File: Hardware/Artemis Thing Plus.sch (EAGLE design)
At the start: 65 parts, among them J2 CORTEX_DEBUG, J5 USB-C, U1 MCP73831, U2 3.3V, U3 ARTEMIS_MODULESMD, U4 CH340E_MSOP10, Y1 32.768kHz

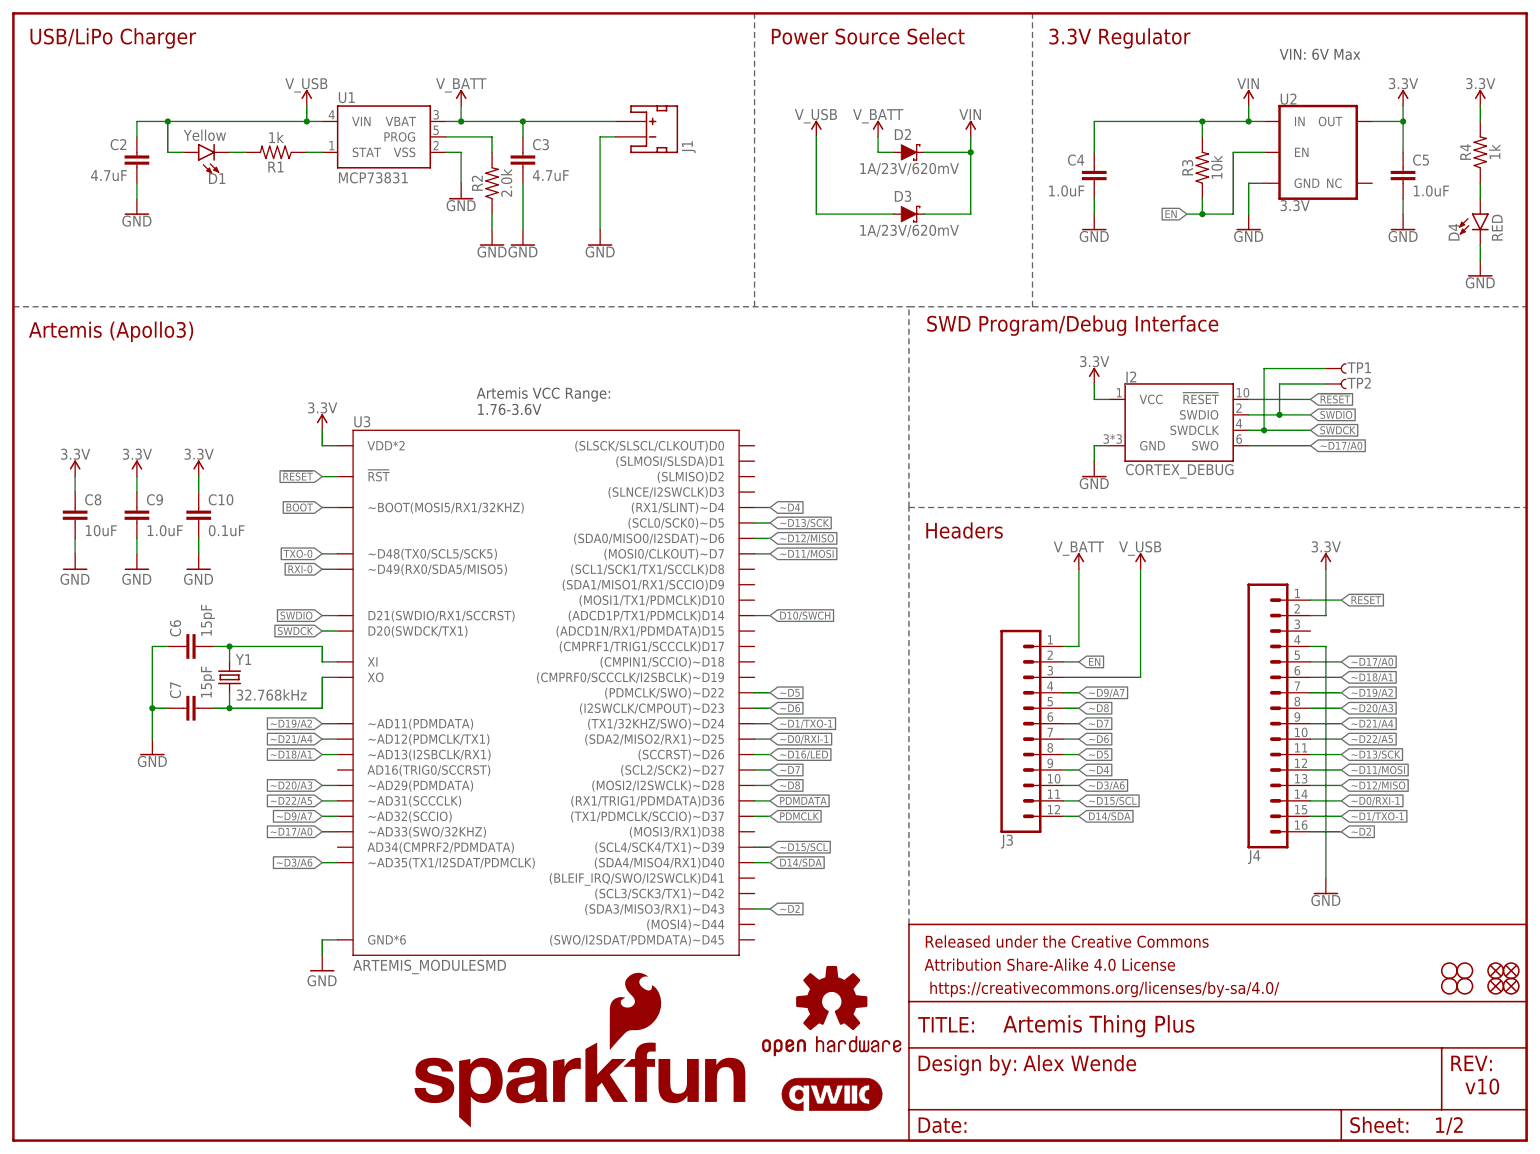
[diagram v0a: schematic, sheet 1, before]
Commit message: v10 Update
Schematic:
- Change 100k pull-down resistor in bootloader circuit to DNP
- Replaced diodes with lower forward voltage drop
- Added second I2C Bus to breakout pins. All broken out pins are now PWM capable
- Replaced 4.7k LEDs resistors to 1k for all LEDs
- Added testpoints for Qwiic data lines

Layout:
- Removed "~" for PWM pins as all pins now support PWM
- Increased flame logo
- Fixed USB traces
- Labeled microphone
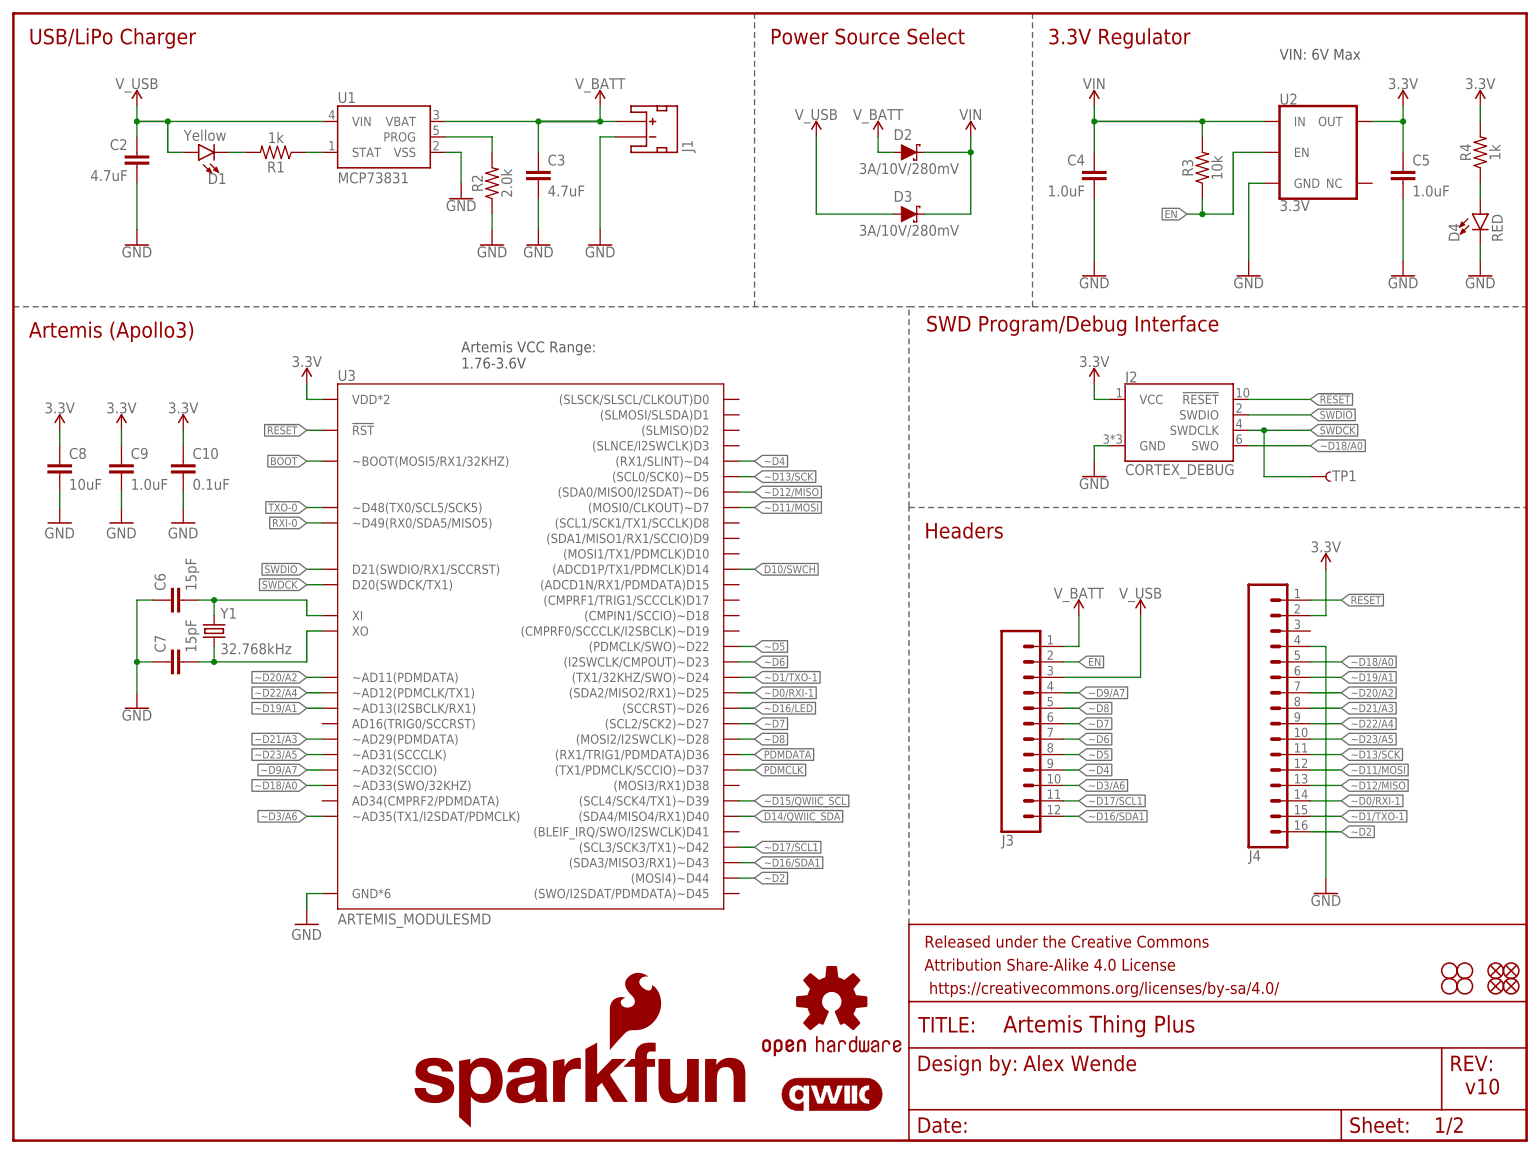
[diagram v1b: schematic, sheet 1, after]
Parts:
- added TP5: TEST-POINTTP_15TH_THRU, SparkFun-Connectors:TEST-POINTTP_15TH_THRU
- D2, D3: value 1A/23V/620mV -> 3A/10V/280mV; device SparkFun-DiscreteSemi:DIODE-SCHOTTKY-BAT20J -> SparkFun-DiscreteSemi:DIODE-SCHOTTKY-BAT60A
- R7, R8: value 4.7k -> 1k; device SparkFun-Resistors:4.7KOHM-0603-1/10W-1% -> SparkFun-Resistors:1KOHM-0603-1/10W-1%
- R9: value 100k -> DNP
- TP1, TP2, TP3, TP4: value TEST-POINT3 -> TEST-POINTTP_15TH_THRU; device SparkFun-Connectors:TEST-POINT3 -> SparkFun-Connectors:TEST-POINTTP_15TH_THRU
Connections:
- net ~D17/A0 renamed ~D18/A0
- net ~D18/A1 renamed ~D19/A1
- net ~D19/A2 renamed ~D20/A2
- net ~D20/A3 renamed ~D21/A3
- net ~D21/A4 renamed ~D22/A4
- net ~D22/A5 renamed ~D23/A5
- removed net D14/SDA: J3.12, J6.3, U3.(SDA4/MISO4/RX1)D40
- removed net ~D15/SCL: J3.11, J6.4, U3.(SCL4/SCK4/TX1)~D39
- new net D14/QWIIC_SDA: J6.3, TP5.1, U3.(SDA4/MISO4/RX1)D40
- new net ~D15/QWIIC_SCL: J6.4, TP4.1, U3.(SCL4/SCK4/TX1)~D39
- new net ~D16/SDA1: J3.12, U3.(SDA3/MISO3/RX1)~D43
- new net ~D17/SCL1: J3.11, U3.(SCL3/SCK3/TX1)~D42
- net RXI-0: now also TP2.1; no longer TP3.1
- net SWDIO: no longer TP2.1
- net TXO-0: now also TP3.1; no longer TP4.1
- net ~D2: now also U3.(MOSI4)~D44; no longer U3.(SDA3/MISO3/RX1)~D43
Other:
- moved on the sheet: C1, C10, C3, C6, C7, C8, C9, TP1, TP3, TP4, U3, Y1

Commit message: v10 design review changes
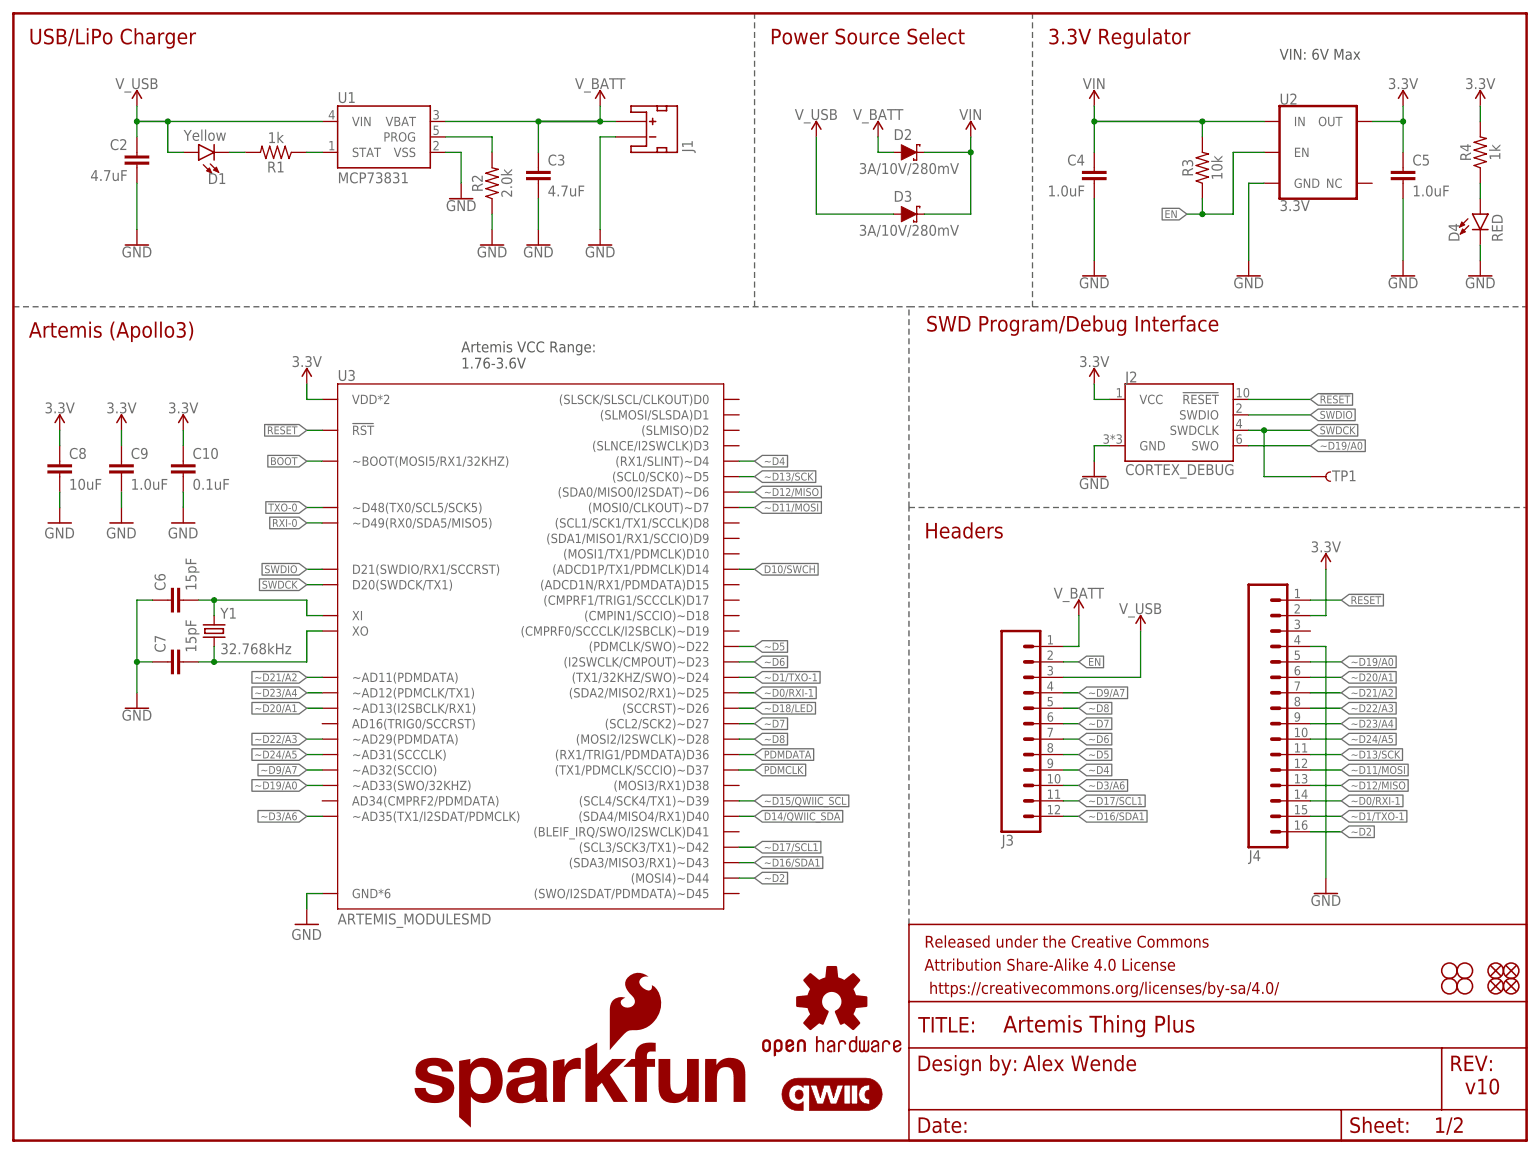
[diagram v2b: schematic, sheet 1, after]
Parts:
- removed R9: DNP, SparkFun-Resistors:100KOHM-0603-1/10W-1%
- C13: value 2.2uF -> 0.1uF; device SparkFun-Capacitors:2.2UF-0603-10V-20% -> SparkFun-Capacitors:0.1UF-0603-25V-5%
- R10: value 10k -> 220k; device SparkFun-Resistors:10KOHM-0603-1/10W-1% -> SparkFun-Resistors:220KOHM-0603-1/10W-1%
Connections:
- net ~D16/LED renamed ~D18/LED
- net ~D18/A0 renamed ~D19/A0
- net ~D19/A1 renamed ~D20/A1
- net ~D20/A2 renamed ~D21/A2
- net ~D21/A3 renamed ~D22/A3
- net ~D22/A4 renamed ~D23/A4
- net ~D23/A5 renamed ~D24/A5
- net !RTS: no longer R9.2
- net GND: no longer R9.1
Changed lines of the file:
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@@
 <part name="C14" library="SparkFun-Capacitors" deviceset="0.1UF" device="-0603-25V-5%" value="0.1uF"/>
 <part name="GND41" library="SparkFun-PowerSymbols" deviceset="GND" device=""/>
-<part name="R10" library="SparkFun-Resistors" deviceset="10KOHM" device="-0603-1/10W-1%" value="10k"/>
-<part name="C13" library="SparkFun-Capacitors" deviceset="2.2UF" device="-0603-10V-20%" value="2.2uF"/>
-<part name="R9" library="SparkFun-Resistors" deviceset="100KOHM" device="-0603-1/10W-1%" value="DNP"/>
-<part name="GND44" library="SparkFun-PowerSymbols" deviceset="GND" device=""/>
+<part name="R10" library="SparkFun-Resistors" deviceset="220KOHM" device="-0603-1/10W-1%" value="220k"/>
+<part name="C13" library="SparkFun-Capacitors" deviceset="0.1UF" device="-0603-25V-5%" value="0.1uF"/>
 <part name="C15" library="SparkFun-Capacitors" deviceset="1.0NF/1000PF" device="-0603-50V-10%" value="1nF"/>
 <part name="GND45" library="SparkFun-PowerSymbols" deviceset="GND" device=""/>
@@
 <attribute name="VALUE" x="175.26" y="89.154" size="1.778" layer="96" font="vector" align="bottom-center"/>
 </instance>
-<instance part="SUPPLY17" gate="G$1" x="185.42" y="86.36" smashed="yes">
-<attribute name="VALUE" x="185.42" y="89.154" size="1.778" layer="96" font="vector" align="bottom-center"/>
+<instance part="SUPPLY17" gate="G$1" x="185.42" y="83.82" smashed="yes">
+<attribute name="VALUE" x="185.42" y="86.614" size="1.778" layer="96" font="vector" align="bottom-center"/>
 </instance>
 </instances>
@@
 <pinref part="J3" gate="G$1" pin="3"/>
 <pinref part="SUPPLY17" gate="G$1" pin="V_USB"/>
-<wire x1="185.42" y1="86.36" x2="185.42" y2="76.2" width="0.1524" layer="91"/>
+<wire x1="185.42" y1="83.82" x2="185.42" y2="76.2" width="0.1524" layer="91"/>
 <wire x1="185.42" y1="76.2" x2="172.72" y2="76.2" width="0.1524" layer="91"/>
 </segment>
@@
 </segment>
 </net>
-<net name="~D22/A4" class="0">
+<net name="~D23/A4" class="0">
 <segment>
 <wire x1="50.8" y1="73.66" x2="48.26" y2="73.66" width="0.1524" layer="91"/>
@@
 </segment>
 </net>
-<net name="~D23/A5" class="0">
+<net name="~D24/A5" class="0">
 <segment>
 <wire x1="50.8" y1="63.5" x2="48.26" y2="63.5" width="0.1524" layer="91"/>
@@
 </segment>
 </net>
-<net name="~D21/A3" class="0">
+<net name="~D22/A3" class="0">
 <segment>
 <wire x1="50.8" y1="66.04" x2="48.26" y2="66.04" width="0.1524" layer="91"/>
@@
 </segment>
 </net>
-<net name="~D20/A2" class="0">
+<net name="~D21/A2" class="0">
 <segment>
 <wire x1="50.8" y1="76.2" x2="48.26" y2="76.2" width="0.1524" layer="91"/>
@@
 </segment>
 </net>
-<net name="~D18/A0" class="0">
+<net name="~D19/A0" class="0">
 <segment>
 <wire x1="50.8" y1="58.42" x2="48.26" y2="58.42" width="0.1524" layer="91"/>
@@
 </segment>
 </net>
-<net name="~D16/LED" class="0">
+<net name="~D18/LED" class="0">
 <segment>
 <pinref part="U3" gate="U1" pin="(SCCRST)~D26"/>
@@
 </segment>
 </net>
-<net name="~D19/A1" class="0">
+<net name="~D20/A1" class="0">
 <segment>
 <pinref part="U3" gate="U1" pin="~AD13(I2SBCLK/RX1)"/>
@@
 <attribute name="VALUE" x="22.479" y="49.784" size="1.778" layer="96" font="vector" rot="R90"/>
 </instance>
-<instance part="R9" gate="G$1" x="12.7" y="40.64" smashed="yes" rot="R90">
-<attribute name="NAME" x="11.176" y="40.64" size="1.778" layer="95" font="vector" rot="R90" align="bottom-center"/>
-<attribute name="VALUE" x="14.224" y="40.64" size="1.778" layer="96" font="vector" rot="R90" align="top-center"/>
-</instance>
-<instance part="GND44" gate="1" x="12.7" y="30.48" smashed="yes" rot="MR0">
-<attribute name="VALUE" x="12.7" y="30.226" size="1.778" layer="96" font="vector" rot="MR0" align="top-center"/>
-</instance>
 <instance part="C15" gate="G$1" x="68.58" y="38.1" smashed="yes">
 <attribute name="NAME" x="70.104" y="41.021" size="1.778" layer="95" font="vector"/>
@@
 <wire x1="25.4" y1="33.02" x2="25.4" y2="35.56" width="0.1524" layer="91"/>
 <pinref part="R10" gate="G$1" pin="1"/>
-</segment>
-<segment>
-<pinref part="R9" gate="G$1" pin="1"/>
-<pinref part="GND44" gate="1" pin="GND"/>
-<wire x1="12.7" y1="33.02" x2="12.7" y2="35.56" width="0.1524" layer="91"/>
 </segment>
 <segment>
@@
 </segment>
 <segment>
-<label x="10.16" y="48.26" size="1.27" layer="95" font="vector" rot="MR0" xref="yes"/>
+<label x="12.7" y="48.26" size="1.27" layer="95" font="vector" rot="MR0" xref="yes"/>
 <pinref part="C13" gate="G$1" pin="1"/>
 <wire x1="15.24" y1="48.26" x2="12.7" y2="48.26" width="0.1524" layer="91"/>
-<pinref part="R9" gate="G$1" pin="2"/>
-<wire x1="12.7" y1="48.26" x2="10.16" y2="48.26" width="0.1524" layer="91"/>
-<wire x1="12.7" y1="45.72" x2="12.7" y2="48.26" width="0.1524" layer="91"/>
-<junction x="12.7" y="48.26"/>
 </segment>
 <segment>
@@
 </segment>
 </net>
-<net name="~D16/LED" class="0">
+<net name="~D18/LED" class="0">
 <segment>
 <pinref part="R12" gate="G$1" pin="2"/>

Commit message: v10 QC fixes
Added + and - symbols to JST connector
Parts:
- FRAME1: DESIGNER (none) -> Alex Wende; REV (none) -> v10
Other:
- note removed: "v10"
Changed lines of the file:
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@@
 </classes>
 <parts>
-<part name="FRAME1" library="SparkFun-Aesthetics" deviceset="FRAME-LETTER" device=""/>
+<part name="FRAME1" library="SparkFun-Aesthetics" deviceset="FRAME-LETTER" device="">
+<attribute name="DESIGNER" value="Alex Wende"/>
+<attribute name="REV" value="v10"/>
+</part>
 <part name="GND13" library="SparkFun-PowerSymbols" deviceset="GND" device=""/>
 <part name="D4" library="SparkFun-LED" deviceset="LED-RED" device="0603" value="RED"/>
@@
 <wire x1="147.32" y1="35.56" x2="147.32" y2="104.14" width="0.1524" layer="97" style="longdash"/>
 <wire x1="147.32" y1="104.14" x2="147.32" y2="137.16" width="0.1524" layer="97" style="longdash"/>
-<text x="238.76" y="7.62" size="2.54" layer="94" font="vector" ratio="15">v10</text>
-<text x="166.116" y="11.43" size="2.54" layer="94" font="vector" ratio="15">Alex Wende</text>
 <wire x1="147.32" y1="104.14" x2="248.92" y2="104.14" width="0.1524" layer="97" style="longdash"/>
 <text x="150.114" y="133.096" size="2.54" layer="94" font="vector" ratio="15">SWD Program/Debug Interface</text>
@@
 <attribute name="SHEET" x="233.68" y="1.27" size="2.54" layer="94" font="vector"/>
 <attribute name="DRAWING_NAME" x="162.814" y="17.78" size="2.7432" layer="94" font="vector"/>
+<attribute name="DESIGNER" x="170.434" y="11.176" size="2.7432" layer="94" font="vector"/>
+<attribute name="REV" x="236.22" y="6.604" size="2.7432" layer="94" font="vector"/>
 </instance>
 <instance part="GND13" gate="1" x="96.52" y="147.32" smashed="yes" rot="MR0">
